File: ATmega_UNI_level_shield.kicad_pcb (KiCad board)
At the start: 2 copper layers, 12.2 x 4.6 mm, 9 parts, among them J11 low, J12 high, J5 pins, Q1 BSS138PS

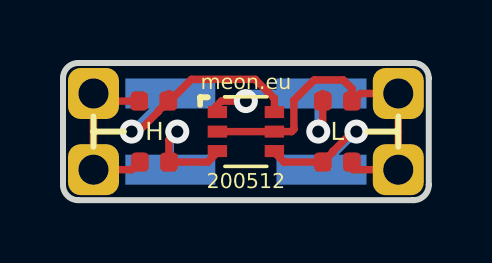
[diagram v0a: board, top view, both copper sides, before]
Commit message: bigger H & L letters
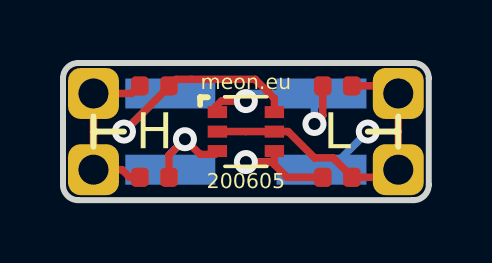
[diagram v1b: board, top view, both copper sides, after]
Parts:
- moved R12 0.51 mm to (122.7, 65.8)
- moved R21 0.51 mm to (128.8, 68.8)
- moved R22 0.51 mm to (122.7, 68.8)
- moved R11 0.51 mm to (128.8, 65.8)
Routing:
- net D2_L: track 5.32 -> 8.15 mm, vias 1 -> 2
- net VIO_L: track 11.9 -> 10.9 mm
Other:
- board text added: "200605"
- board text removed: "200512"
